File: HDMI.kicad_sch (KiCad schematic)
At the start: 5 parts, among them J9 HDMI_E, U1 RT9742SNGV

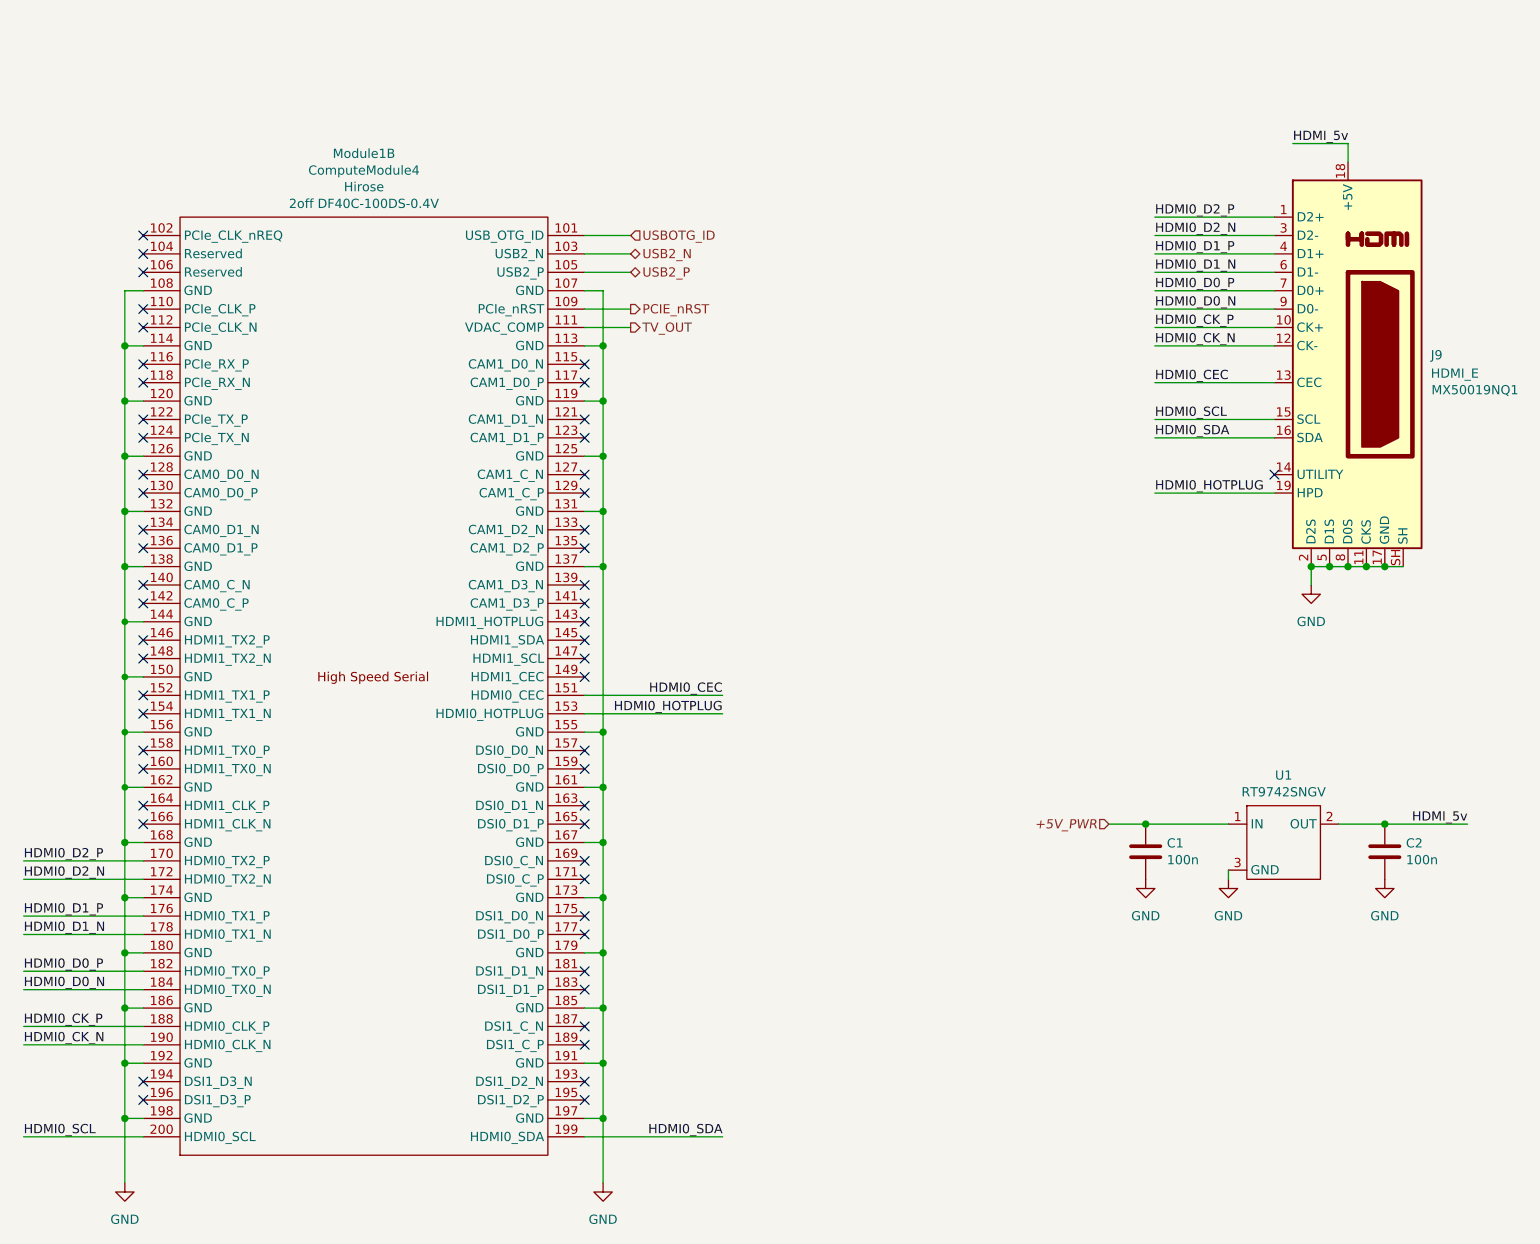
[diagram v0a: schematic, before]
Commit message: power dist, hdmi, and rtc are done; finding a new usb hub
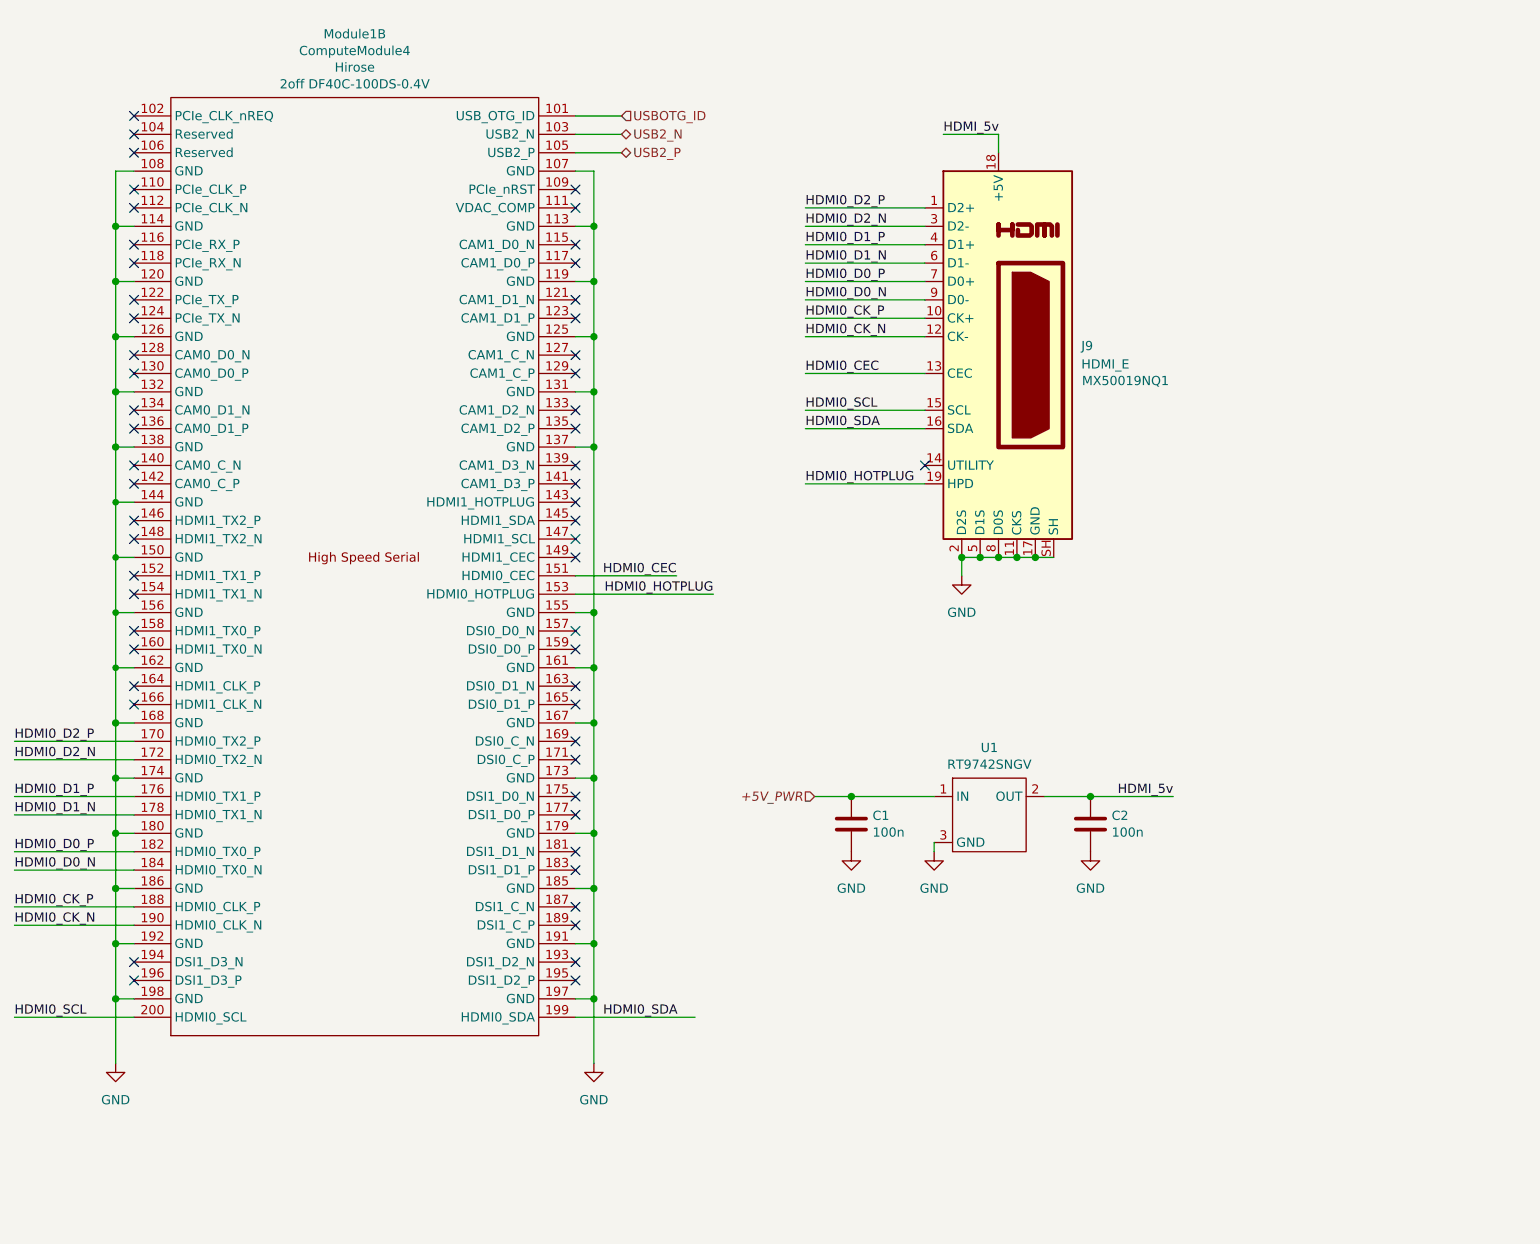
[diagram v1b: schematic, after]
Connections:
- net PCIE_nRST: no longer names the net of Module1.109 (PCIe_nRST)
- net TV_OUT: no longer names the net of Module1.111 (VDAC_COMP)
- no-connect marks 54 -> 56
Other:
- moved on the sheet: C2, J9, Module1B

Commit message: made more changes
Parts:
- removed U1: RT9742SNGV, Package_TO_SOT_SMD:SOT-23, symbol CM4IO:RT9742SNGV
- added U5: RT9742SNGV, symbol CM4IO:RT9742SNGV
- Module1: value ComputeModule4 -> ComputeModule4-CM4; Field5 2off DF40C-100DS-0.4V -> 2x DF40C-100DS-0.4V; Field6 2off DF40C-100DS-0.4V -> (none); Field7 Hirose -> (none); Part Description 100 Position Connector Receptacle, Center Strip Contacts Su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 -> (none)
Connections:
- net +5V_PWR: now also U5.1 (IN)
- net GND: now also U5.3 (GND)
- net HDMI_5v: now also U5.2 (OUT)

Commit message: finished USB i think, working on general gpio in more detail
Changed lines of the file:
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@@
 	(wire
 		(pts
-			(xy 100.33 87.63) (xy 114.3 87.63)
+			(xy 100.33 87.63) (xy 119.38 87.63)
 		)
 		(stroke
@@
 	(wire
 		(pts
-			(xy 100.33 148.59) (xy 116.84 148.59)
+			(xy 100.33 148.59) (xy 119.38 148.59)
 		)
 		(stroke
@@
 		)
 	)
+	(label "HDMI0_SDA"
+		(at 119.38 148.59 180)
+		(fields_autoplaced yes)
+		(effects
+			(font
+				(size 1.27 1.27)
+			)
+			(justify right bottom)
+		)
+	)
 	(label "HDMI0_D0_P"
 		(at 22.86 125.73 0)
@@
 	)
 	(label "HDMI0_CEC"
-		(at 114.3 87.63 180)
+		(at 119.38 87.63 180)
 		(fields_autoplaced yes)
 		(effects
@@
 		(fields_autoplaced yes)
 		(effects
-			(font
-				(size 1.27 1.27)
-			)
-			(justify left bottom)
-		)
-	)
-	(label "HDMI0_SDA"
-		(at 104.14 148.59 0)
-		(fields_autoplaced yes)
-		(effects

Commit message: we ballin??
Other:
- moved on the sheet: C1, C2, J9, U5
